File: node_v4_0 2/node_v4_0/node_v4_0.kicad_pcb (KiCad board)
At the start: 4 copper layers, 45.7 x 76.2 mm, 98 parts, among them J1 Conn_01x02_Pin, J2 12402012E212A, J3 Conn_Coaxial, J4 Conn_02x08_Odd_Even, J5 Conn_02x02_Odd_Even, J6 GNSS_ANT, J7 RF_ANT, Q1 DMG2301L, Q2 DMG2301L, U1 RP2040, U10 MCP7940 / DS1307 / PCF8523, U11 1042240820, U12 CAT24M01W, U13 MAX31342EWA+T, U2 W25Q128JVS, U3 AP2112K-3.3, U4 CAT3200-5, U5 MCP73831-2-OT, U6 RFM69HCW, U7 PTS526 SK15 SMTR2 LFS, U8 PTS526 SK15 SMTR2 LFS, U9 SIM7080G

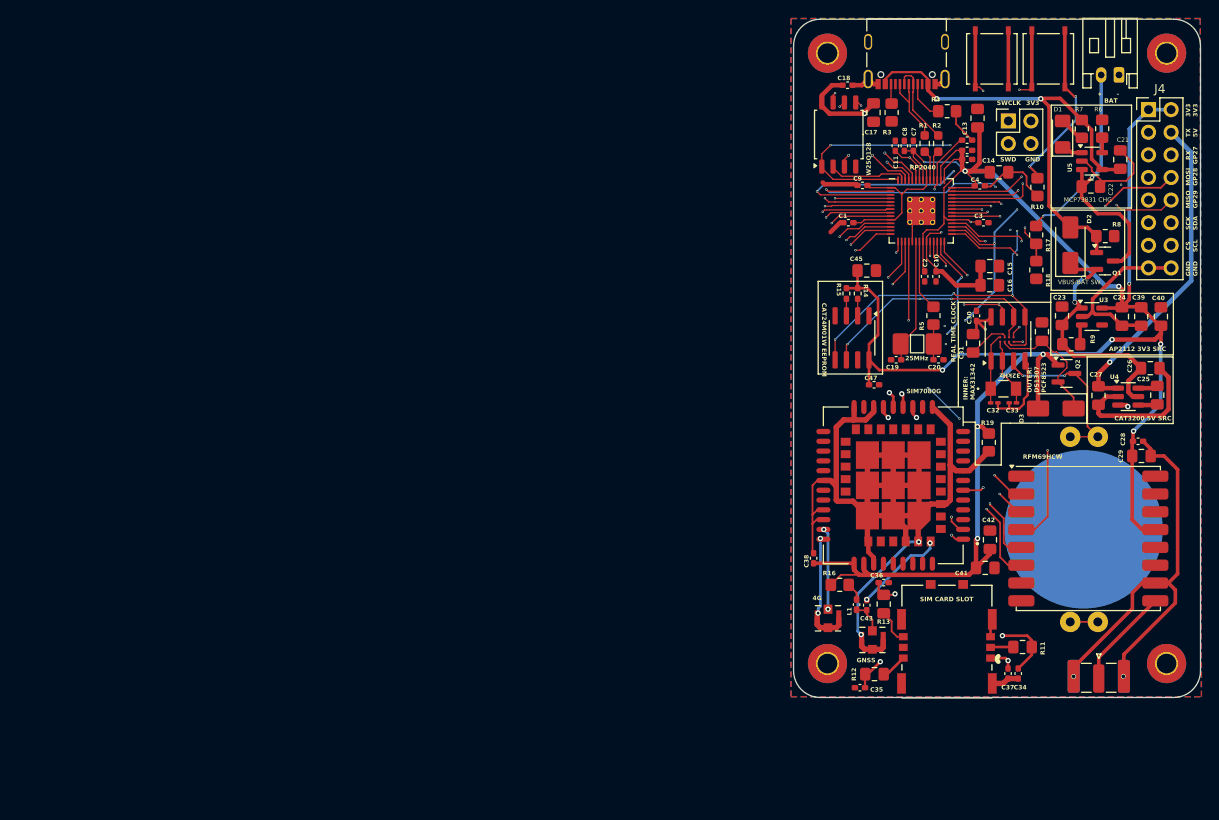
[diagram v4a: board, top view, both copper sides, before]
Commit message: added vin for solar/charge, more minor fixes
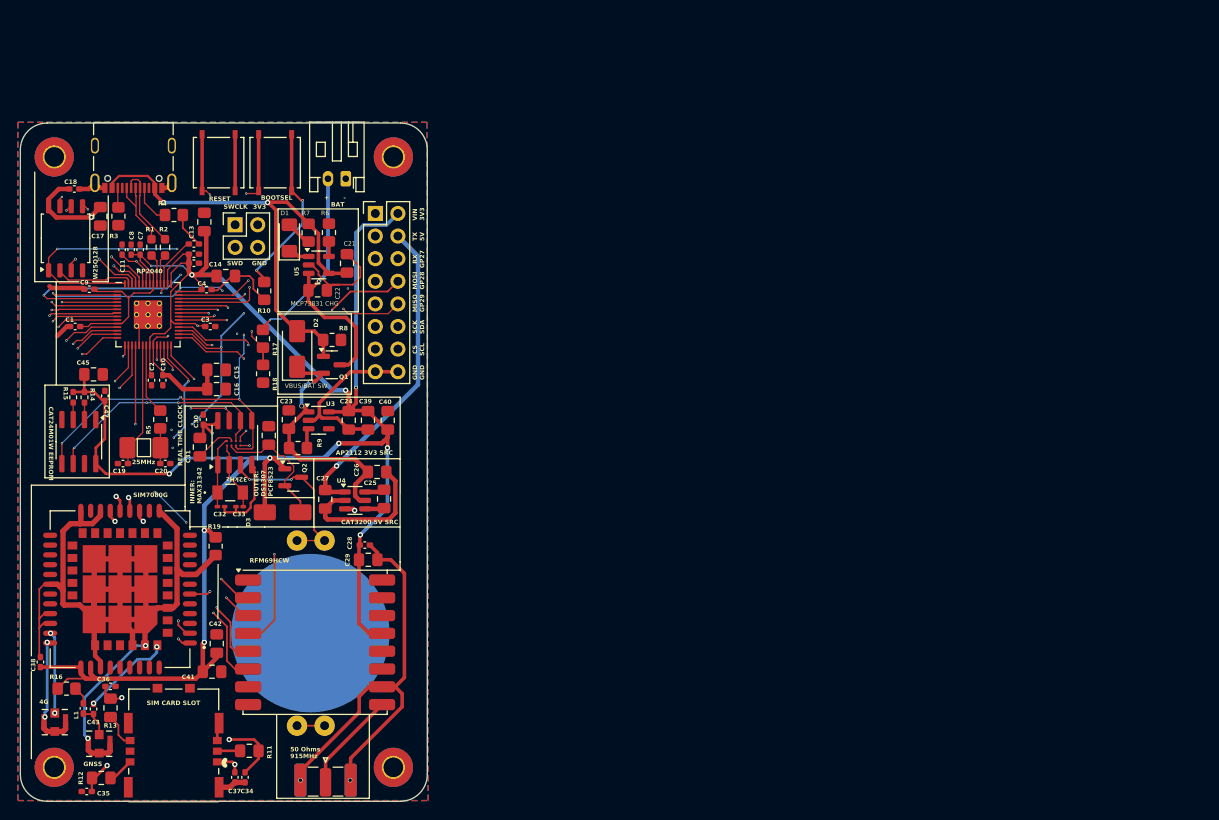
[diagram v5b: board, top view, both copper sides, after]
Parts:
- added G***: LOGO, WiSDOM:prince, B.Cu at (42.0, 55.5)
- added G***: LOGO, logos:wisdom_logo_lineborder, B.Cu at (48.9, 56.2)
- added LOGO: , logos:qrcode, B.Cu at (41.9, 84.2)
- added LOGO: , logos:github_qr, B.Cu at (41.8, 95.2)
- moved C10 87.6 mm to (40.0, 58.7)
- moved C11 87.6 mm to (35.5, 44.0)
- moved C12 87.6 mm to (43.5, 43.4)
- moved C13 87.6 mm to (44.7, 40.9)
- moved C14 87.6 mm to (47.1, 47.0)
- moved C17 87.6 mm to (33.0, 40.3)
- moved C18 87.6 mm to (30.1, 37.2)
- moved C19 87.6 mm to (35.6, 68.0)
- moved C2 87.6 mm to (38.8, 58.7)
- moved C20 87.6 mm to (40.3, 68.0)
- moved C21 87.6 mm to (60.7, 45.5)
- moved C22 87.6 mm to (57.4, 48.6)
- moved C23 87.6 mm to (54.2, 63.1)
- moved C24 87.6 mm to (60.9, 63.2)
- moved C25 87.6 mm to (64.9, 72.0)
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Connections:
- J4 pad 1: +3.3V -> VBUS
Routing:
- net VBUS: track 55.9 -> 68.5 mm
- net +3.3V: track 343.1 -> 340.3 mm
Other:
- board text added: "50 Ohms"
- board text added: "915MHz"
- board text added: "BOOTSEL"
- board text added: "Design by Amelia Vlahogiannis 2024"
- board text added: "RESET"
- board text added: "VIN 3V3"
- board text added: "WiSDOM GitHub"
- board text added: "WiSDOM Node Version 4.0 Design Rev. 2 With Cellular"
- board text added: "wisdomresearch.net"
- board text removed: "3V3 3V3"

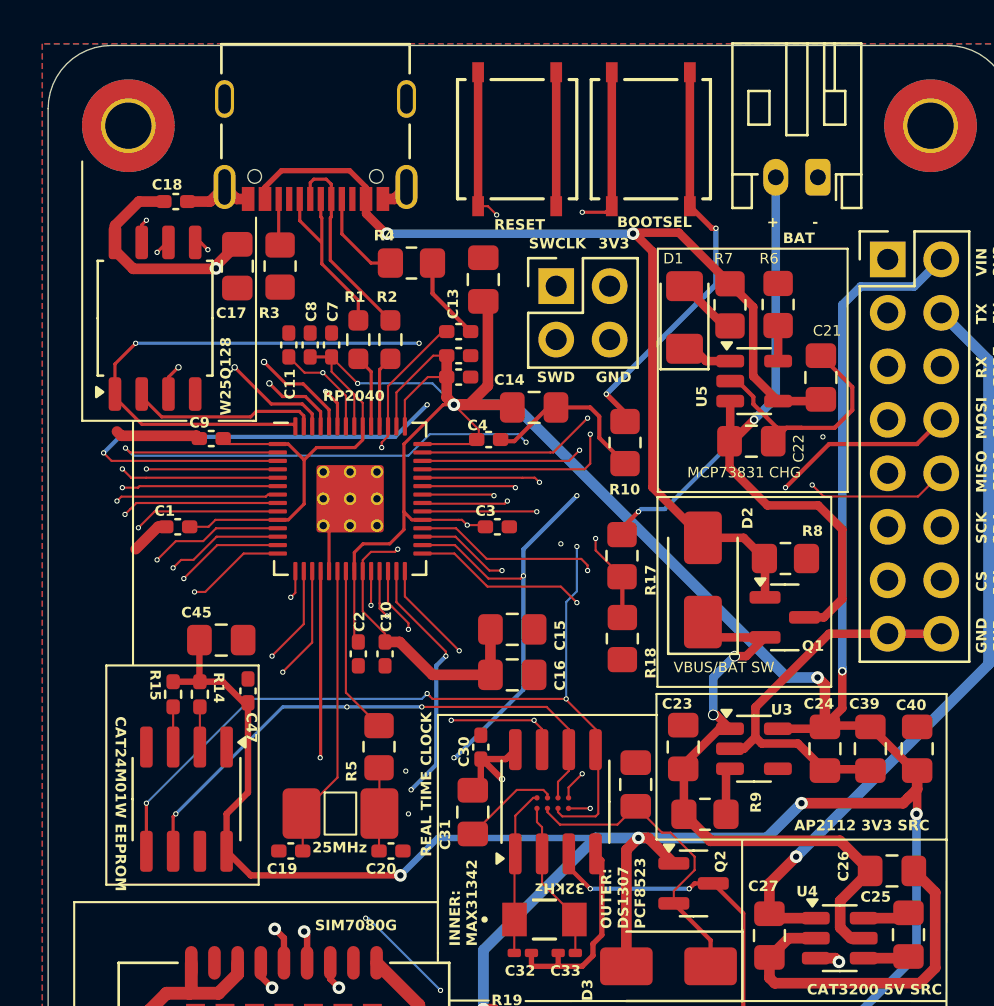
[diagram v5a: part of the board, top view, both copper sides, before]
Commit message: moved reset button to make space for vin jst connector
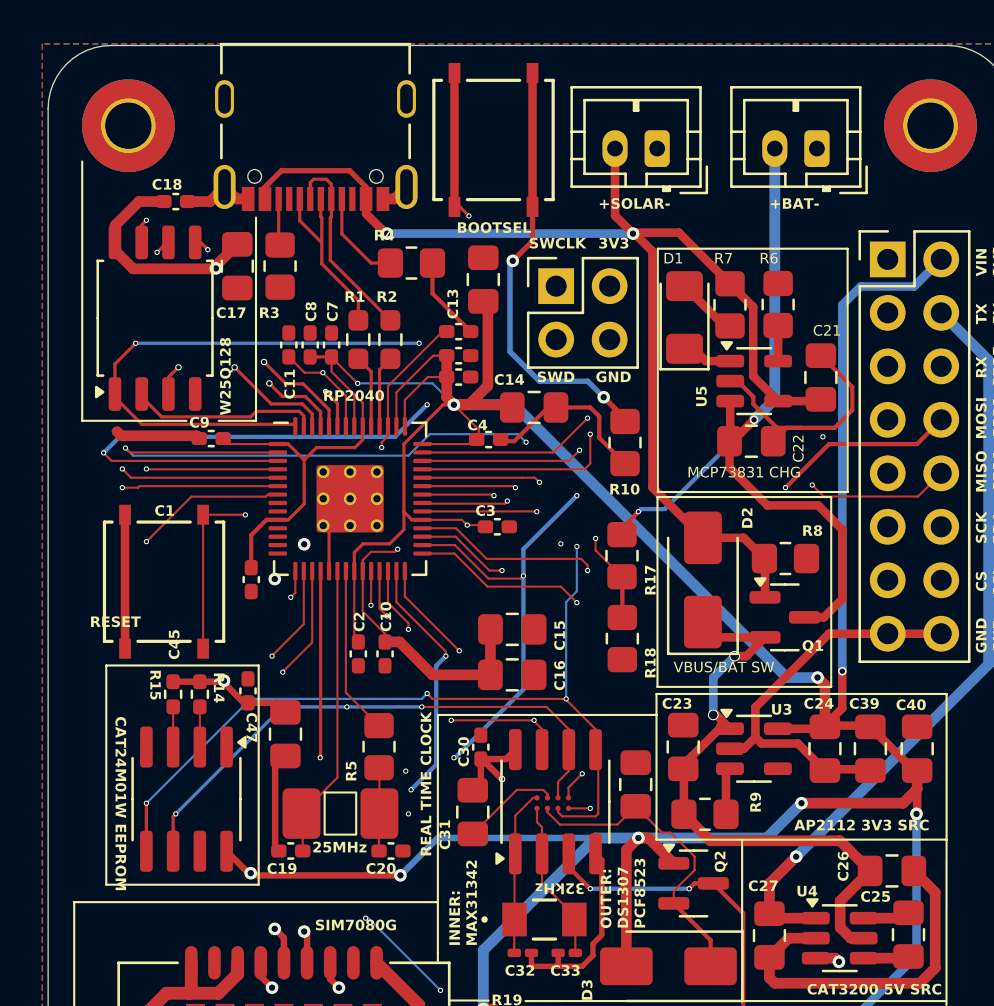
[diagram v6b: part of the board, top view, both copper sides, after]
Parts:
- added J8: Conn_01x02_Pin, Connector_JST:JST_PH_B2B-PH-K_1x02_P2.00mm_Vertical, F.Cu at (53.0, 34.7)
- J1: footprint Connector_JST:JST_PH_S2B-PH-K_1x02_P2.00mm_Horizontal -> Connector_JST:JST_PH_B2B-PH-K_1x02_P2.00mm_Vertical
- R10: value R -> 10k
- R19: value 100k -> 10k
- R7: value R -> 1k
- moved U7 26.9 mm to (29.5, 55.2), turned to -90 degrees
- moved U8 7.47 mm to (45.2, 34.3)
- moved C45 5.41 mm to (35.3, 62.5), turned to -90 degrees
- moved C1 4.30 mm to (33.7, 55.1), turned to -90 degrees
- moved J1 1.37 mm to (60.5, 34.7)
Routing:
- net /MCU/RESET: track 32.0 -> 21.6 mm
- net unconnected-(U1-GPIO6-Pad8): track 7.48 -> 0.00 mm, vias 1 -> 0
- net unconnected-(U1-GPIO7-Pad9): track 6.94 -> 0.00 mm, vias 1 -> 0
- net unconnected-(U1-GPIO8-Pad11): track 6.35 -> 0.00 mm, vias 1 -> 0
- net unconnected-(U1-GPIO9-Pad12): track 5.58 -> 0.00 mm, vias 1 -> 0
- net unconnected-(U1-GPIO10-Pad13): track 5.12 -> 0.00 mm, vias 1 -> 0
- net unconnected-(U1-GPIO11-Pad14): track 4.71 -> 0.00 mm, vias 1 -> 0
- net VBUS: track 68.5 -> 72.9 mm
- net GND: track 286.1 -> 289.4 mm, vias 6 -> 8
- net /MCU/CS: track 43.8 -> 40.7 mm
- net SCL: track 77.3 -> 74.5 mm
- net +3.3V: track 340.3 -> 341.7 mm, vias 14 -> 16
- net +BATT: track 37.4 -> 38.8 mm
- net Net-(R10-Pad1): track 19.7 -> 21.0 mm
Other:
- board text added: "+BAT-"
- board text added: "+SOLAR-"
- board text removed: "+"
- board text removed: "-"
- board text removed: "BAT"
